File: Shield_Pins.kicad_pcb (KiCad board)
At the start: 2 copper layers, 76 x 38.3 mm, 9 parts, among them J1 Conn_01x04_Male, J2 Conn_01x06_Male, J3 Conn_01x06_Male, J4 Conn_01x04_Male, J5 Conn_01x01_Male, J6 Conn_01x06_Male, J7 Conn_01x15_Male, J8 Conn_01x15_Male, J9 Conn_01x02_Male

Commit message: shield
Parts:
- added D1: IR204A, LED_THT:LED_D3.0mm_IRBlack, F.Cu at (92.5, 93.8)
- added LS1: PS1240P02BT, Sensor:PS1240P02BT, F.Cu at (150.5, 96.5)
- added R1: A1050, OptoDevice:R_LDR_D6.4mm_P3.4mm_Vertical, F.Cu at (135.0, 99.7)
- added R2: 10K, Resistor_SMD:R_0805_2012Metric_Pad1.20x1.40mm_HandSolder, F.Cu at (140.0, 97.5)
- added R3: 100, Resistor_SMD:R_0805_2012Metric_Pad1.20x1.40mm_HandSolder, F.Cu at (97.0, 91.0)
- added U1: HC-SR04, Sensor:HC-SR04, F.Cu at (101.5, 99.0)
- added U2: DHT22, Sensor:DHT22_Temperature_Humidity, F.Cu at (104.5, 75.5)
- added U3: TSOP1738, OptoDevice:Vishay_CAST-3Pin, F.Cu at (94.3, 78.7)
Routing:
- net IO17: track 0.00 -> 66.8 mm
- net IO12: track 0.00 -> 62.4 mm
- net IO8: track 0.00 -> 62.0 mm
- net IO9: track 0.00 -> 59.9 mm
- net IO18: track 0.00 -> 59.0 mm
- net IO11: track 0.00 -> 26.9 mm
- net IO10: track 0.00 -> 13.0 mm
- net Net-(D1-Pad2): track 0.00 -> 3.60 mm
- net GND: track 0.00 -> 2.00 mm, vias 0 -> 1
- added copper zone on F.Cu, net +5V
- added copper zone on B.Cu, net GND

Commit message: Add files via upload
minor fixes
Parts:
- added R4: 10K, Resistor_SMD:R_0805_2012Metric_Pad1.20x1.40mm_HandSolder, F.Cu at (104.8, 80.5)
- moved R2 0.56 mm to (139.5, 97.2)
- moved R3 0.25 mm to (97.0, 91.2)
- turned LS1 to 180 degrees
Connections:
- LS1 pad 1: IO10 -> IO9
- R1 pad 2: IO11 -> IO8
- R2 pad 1: IO11 -> IO8
- R3 pad 2: IO12 -> IO18
- U1 pad 2: IO8 -> IO17
- U1 pad 3: IO9 -> IO10
- U2 pad 2: IO18 -> IO20
- U3 pad 3: IO17 -> IO19
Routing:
- net IO19: track 0.00 -> 66.6 mm
- net IO12: track 62.4 -> 0.00 mm
- net IO20: track 0.00 -> 60.3 mm
- net IO9: track 59.9 -> 7.21 mm
- net IO10: track 13.0 -> 59.2 mm
- net IO8: track 62.0 -> 26.2 mm
- net IO11: track 26.9 -> 0.00 mm
- net GND: track 2.00 -> 8.49 mm, vias 1 -> 0
- net IO18: track 59.0 -> 64.1 mm
- net IO17: track 66.8 -> 65.1 mm

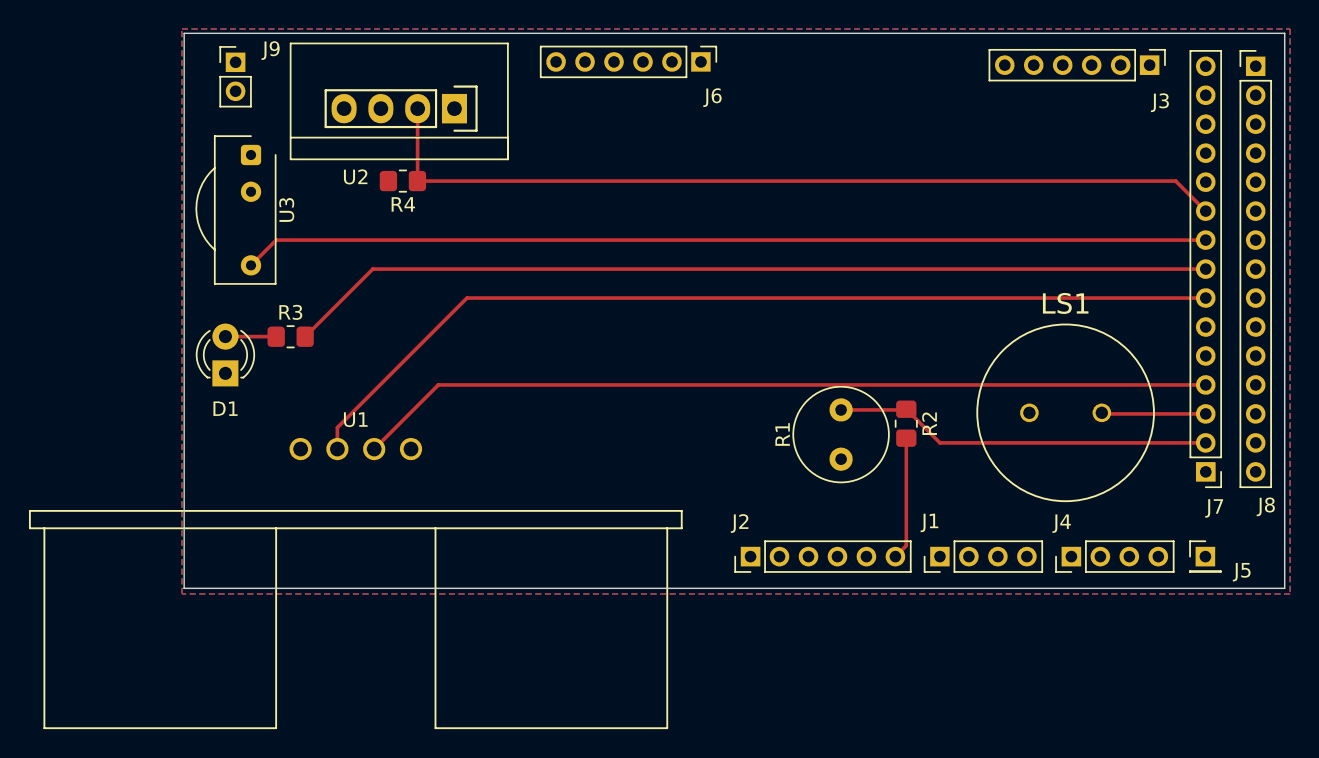
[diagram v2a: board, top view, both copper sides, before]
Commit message: added top and bottom gnd layer
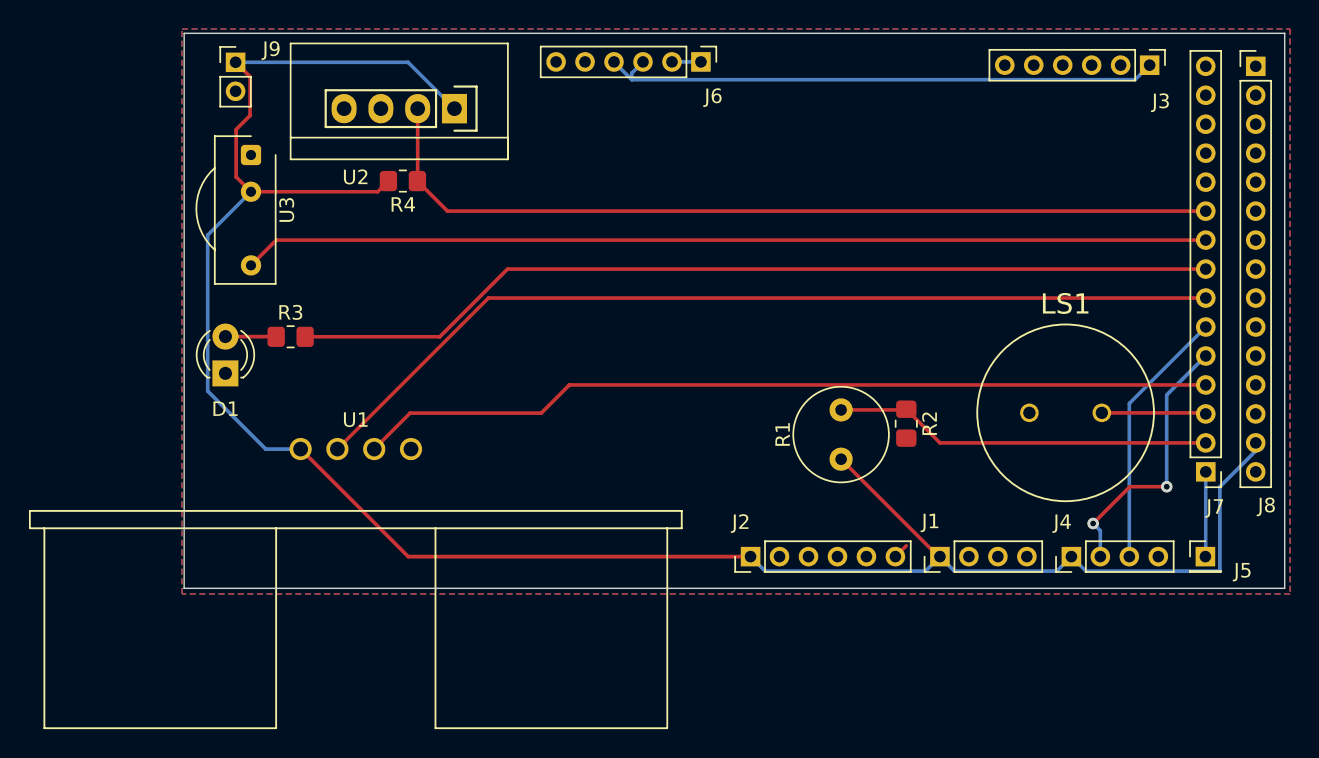
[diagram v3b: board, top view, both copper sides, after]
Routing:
- net +5V: track 0.00 -> 147.5 mm
- net +3.3V: track 0.00 -> 39.4 mm
- net IO11: track 0.00 -> 18.8 mm, vias 0 -> 2
- net IO12: track 0.00 -> 18.0 mm
- net GND: track 8.49 -> 1.06 mm
- net IO7: track 0.00 -> 5.86 mm
- net +1V8: track 0.00 -> 2.00 mm
- net IO17: track 65.1 -> 64.3 mm
- added copper zone on F.Cu, net GND
- removed copper zone on F.Cu, net +5V
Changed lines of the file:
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@@
     (style (thickness 0.1) (arrow_length 1.27) (text_position_mode 0) (extension_height 0.58642) (extension_offset 0.5) keep_text_aligned)
   )
-  (segment (start 139.5 98.25) (end 139.5 105.675) (width 0.25) (layer "F.Cu") (net 4))
+  (segment (start 135 99.7) (end 141.725 106.425) (width 0.25) (layer "F.Cu") (net 1))
+  (segment (start 103.75 80.5) (end 103.01 81.24) (width 0.25) (layer "F.Cu") (net 1))
+  (segment (start 93.24 76.94) (end 94.2 75.98) (width 0.25) (layer "F.Cu") (net 1))
+  (segment (start 141.725 106.425) (end 141.825 106.425) (width 0.25) (layer "F.Cu") (net 1))
+  (segment (start 105.115 106.425) (end 97.69 99) (width 0.25) (layer "F.Cu") (net 1))
+  (segment (start 128.75 106.425) (end 105.115 106.425) (width 0.25) (layer "F.Cu") (net 1))
+  (segment (start 93.24 80.215) (end 93.24 76.94) (width 0.25) (layer "F.Cu") (net 1))
+  (segment (start 94.265 81.24) (end 93.24 80.215) (width 0.25) (layer "F.Cu") (net 1))
+  (segment (start 94.2 73.3) (end 93.2 72.3) (width 0.25) (layer "F.Cu") (net 1))
+  (segment (start 103.01 81.24) (end 94.265 81.24) (width 0.25) (layer "F.Cu") (net 1))
+  (segment (start 94.2 75.98) (end 94.2 73.3) (width 0.25) (layer "F.Cu") (net 1))
+  (segment (start 163.625 99.125) (end 161.15 101.6) (width 0.25) (layer "B.Cu") (net 1))
+  (segment (start 108.31 75.5) (end 105.11 72.3) (width 0.25) (layer "B.Cu") (net 1))
+  (segment (start 161.085 107.425) (end 151.9 107.425) (width 0.25) (layer "B.Cu") (net 1))
+  (segment (start 91.275 84.23) (end 94.265 81.24) (width 0.25) (layer "B.Cu") (net 1))
+  (segment (start 142.825 107.425) (end 141.825 106.425) (width 0.25) (layer "B.Cu") (net 1))
+  (segment (start 149.9 107.425) (end 142.825 107.425) (width 0.25) (layer "B.Cu") (net 1))
+  (segment (start 150.9 106.425) (end 149.9 107.425) (width 0.25) (layer "B.Cu") (net 1))
+  (segment (start 97.69 99) (end 95.275 99) (width 0.25) (layer "B.Cu") (net 1))
+  (segment (start 91.275 95) (end 91.275 84.23) (width 0.25) (layer "B.Cu") (net 1))
+  (segment (start 140.825 107.425) (end 129.75 107.425) (width 0.25) (layer "B.Cu") (net 1))
+  (segment (start 151.9 107.425) (end 150.9 106.425) (width 0.25) (layer "B.Cu") (net 1))
+  (segment (start 95.275 99) (end 91.275 95) (width 0.25) (layer "B.Cu") (net 1))
+  (segment (start 161.15 101.6) (end 161.15 107.36) (width 0.25) (layer "B.Cu") (net 1))
+  (segment (start 129.75 107.425) (end 128.75 106.425) (width 0.25) (layer "B.Cu") (net 1))
+  (segment (start 163.625 98.575) (end 163.625 99.125) (width 0.25) (layer "B.Cu") (net 1))
+  (segment (start 141.825 106.425) (end 140.825 107.425) (width 0.25) (layer "B.Cu") (net 1))
+  (segment (start 105.11 72.3) (end 93.2 72.3) (width 0.25) (layer "B.Cu") (net 1))
+  (segment (start 161.15 107.36) (end 161.085 107.425) (width 0.25) (layer "B.Cu") (net 1))
   (segment (start 139.5 105.675) (end 138.75 106.425) (width 0.25) (layer "F.Cu") (net 4))
+  (segment (start 120.55 73.05) (end 120.55 73.5) (width 0.25) (layer "B.Cu") (net 9))
+  (segment (start 155.3 73.5) (end 156.3 72.5) (width 0.25) (layer "B.Cu") (net 9))
+  (segment (start 119.325 72.275) (end 120.55 73.5) (width 0.25) (layer "B.Cu") (net 9))
+  (segment (start 120.55 73.5) (end 155.3 73.5) (width 0.25) (layer "B.Cu") (net 9))
+  (segment (start 121.325 72.275) (end 120.55 73.05) (width 0.25) (layer "B.Cu") (net 9))
+  (segment (start 152.4 104.14) (end 154.94 101.6) (width 0.25) (layer "F.Cu") (net 14))
+  (segment (start 154.94 101.6) (end 157.48 101.6) (width 0.25) (layer "F.Cu") (net 14))
+  (via (at 157.48 101.6) (size 0.8) (drill 0.4) (layers "F.Cu" "B.Cu") (net 14))
+  (via (at 152.4 104.14) (size 0.8) (drill 0.4) (layers "F.Cu" "B.Cu") (net 14))
+  (segment (start 152.9 106.425) (end 152.9 104.64) (width 0.25) (layer "B.Cu") (net 14))
+  (segment (start 157.48 101.6) (end 157.48 95.27) (width 0.25) (layer "B.Cu") (net 14))
+  (segment (start 152.9 104.64) (end 152.4 104.14) (width 0.25) (layer "B.Cu") (net 14))
+  (segment (start 157.48 95.27) (end 160.175 92.575) (width 0.25) (layer "B.Cu") (net 14))
+  (segment (start 154.9 95.85) (end 154.9 106.425) (width 0.25) (layer "B.Cu") (net 15))
+  (segment (start 160.175 90.575) (end 154.9 95.85) (width 0.25) (layer "B.Cu") (net 15))
+  (segment (start 160.175 106.4) (end 160.15 106.425) (width 0.25) (layer "B.Cu") (net 16))
+  (segment (start 160.175 100.575) (end 160.175 106.4) (width 0.25) (layer "B.Cu") (net 16))
+  (segment (start 123.325 72.275) (end 125.325 72.275) (width 0.25) (layer "B.Cu") (net 17))
+  (segment (start 141.825 98.575) (end 160.175 98.575) (width 0.25) (layer "F.Cu") (net 18))
   (segment (start 135 96.3) (end 139.45 96.3) (width 0.25) (layer "F.Cu") (net 18))
   (segment (start 139.45 96.3) (end 139.5 96.25) (width 0.25) (layer "F.Cu") (net 18))
-  (segment (start 141.825 98.575) (end 139.5 96.25) (width 0.25) (layer "F.Cu") (net 18))
-  (segment (start 160.175 98.575) (end 141.825 98.575) (width 0.25) (layer "F.Cu") (net 18))
-  (segment (start 153.075 96.575) (end 153 96.5) (width 0.25) (layer "F.Cu") (net 19))
-  (segment (start 160.175 96.575) (end 153.075 96.575) (width 0.25) (layer "F.Cu") (net 19))
-  (segment (start 102.77 99) (end 107.195 94.575) (width 0.25) (layer "F.Cu") (net 20))
-  (segment (start 107.195 94.575) (end 160.175 94.575) (width 0.25) (layer "F.Cu") (net 20))
-  (segment (start 109.175 88.575) (end 160.175 88.575) (width 0.25) (layer "F.Cu") (net 21))
-  (segment (start 100.23 97.52) (end 109.175 88.575) (width 0.25) (layer "F.Cu") (net 21))
-  (segment (start 100.23 99) (end 100.23 97.52) (width 0.25) (layer "F.Cu") (net 21))
-  (segment (start 98 91.25) (end 102.675 86.575) (width 0.25) (layer "F.Cu") (net 22))
-  (segment (start 102.675 86.575) (end 160.175 86.575) (width 0.25) (layer "F.Cu") (net 22))
-  (segment (start 96.01 84.575) (end 94.265 86.32) (width 0.25) (layer "F.Cu") (net 23))
-  (segment (start 160.175 84.575) (end 96.01 84.575) (width 0.25) (layer "F.Cu") (net 23))
-  (segment (start 158.1 80.5) (end 160.175 82.575) (width 0.25) (layer "F.Cu") (net 24))
-  (segment (start 105.77 75.5) (end 105.77 80.48) (width 0.25) (layer "F.Cu") (net 24))
-  (segment (start 105.77 80.48) (end 105.75 80.5) (width 0.25) (layer "F.Cu") (net 24))
-  (segment (start 105.75 80.5) (end 158.1 80.5) (width 0.25) (layer "F.Cu") (net 24))
+  (segment (start 139.5 96.25) (end 141.825 98.575) (width 0.25) (layer "F.Cu") (net 18))
+  (segment (start 153 96.5) (end 160.1 96.5) (width 0.25) (layer "F.Cu") (net 19))
+  (segment (start 160.1 96.5) (end 160.175 96.575) (width 0.25) (layer "F.Cu") (net 19))
+  (segment (start 114.3 96.52) (end 116.245 94.575) (width 0.25) (layer "F.Cu") (net 20))
+  (segment (start 102.77 99) (end 105.25 96.52) (width 0.25) (layer "F.Cu") (net 20))
+  (segment (start 116.245 94.575) (end 160.175 94.575) (width 0.25) (layer "F.Cu") (net 20))
+  (segment (start 105.25 96.52) (end 114.3 96.52) (width 0.25) (layer "F.Cu") (net 20))
+  (segment (start 110.655 88.575) (end 160.175 88.575) (width 0.25) (layer "F.Cu") (net 21))
+  (segment (start 100.23 99) (end 110.655 88.575) (width 0.25) (layer "F.Cu") (net 21))
+  (segment (start 160.175 86.575) (end 111.975 86.575) (width 0.25) (layer "F.Cu") (net 22))
+  (segment (start 111.975 86.575) (end 107.3 91.25) (width 0.25) (layer "F.Cu") (net 22))
+  (segment (start 107.3 91.25) (end 98 91.25) (width 0.25) (layer "F.Cu") (net 22))
+  (segment (start 96.01 84.575) (end 160.175 84.575) (width 0.25) (layer "F.Cu") (net 23))
+  (segment (start 94.265 86.32) (end 96.01 84.575) (width 0.25) (layer "F.Cu") (net 23))
+  (segment (start 105.75 80.5) (end 105.77 80.48) (width 0.25) (layer "F.Cu") (net 24))
+  (segment (start 107.825 82.575) (end 160.175 82.575) (width 0.25) (layer "F.Cu") (net 24))
+  (segment (start 105.75 80.5) (end 107.825 82.575) (width 0.25) (layer "F.Cu") (net 24))
+  (segment (start 105.77 80.48) (end 105.77 75.5) (width 0.25) (layer "F.Cu") (net 24))
   (segment (start 92.5 91.235) (end 95.985 91.235) (width 0.25) (layer "F.Cu") (net 43))
   (segment (start 95.985 91.235) (end 96 91.25) (width 0.25) (layer "F.Cu") (net 43))
-  (zone (net 1) (net_name "+5V") (layer "F.Cu") (hatch edge 0.508)
+  (zone (net 4) (net_name "GND") (layer "F.Cu") (hatch edge 0.508)
     (connect_pads (clearance 0.508))
     (min_thickness 0.254) (filled_areas_thickness no)
